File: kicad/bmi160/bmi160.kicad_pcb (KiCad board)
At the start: 2 copper layers, 31 x 42 mm, 41 parts, among them J1 USB4125-GF-A_REVA, J2 PinHeader_2x03_P2.54mm_Vertic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, J3 PinHeader_1x05_P2.54mm_Vertic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, J4 PinHeader_1x02_P2.54mm_Vertic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, SW1 SW_SPDT, U1 dfn-8_wide, U2 BQ297xy, U3 CSD85302L, U4 NCP177BMX330TCG, U5 ASAK-32.7680KHZ-LRS-T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

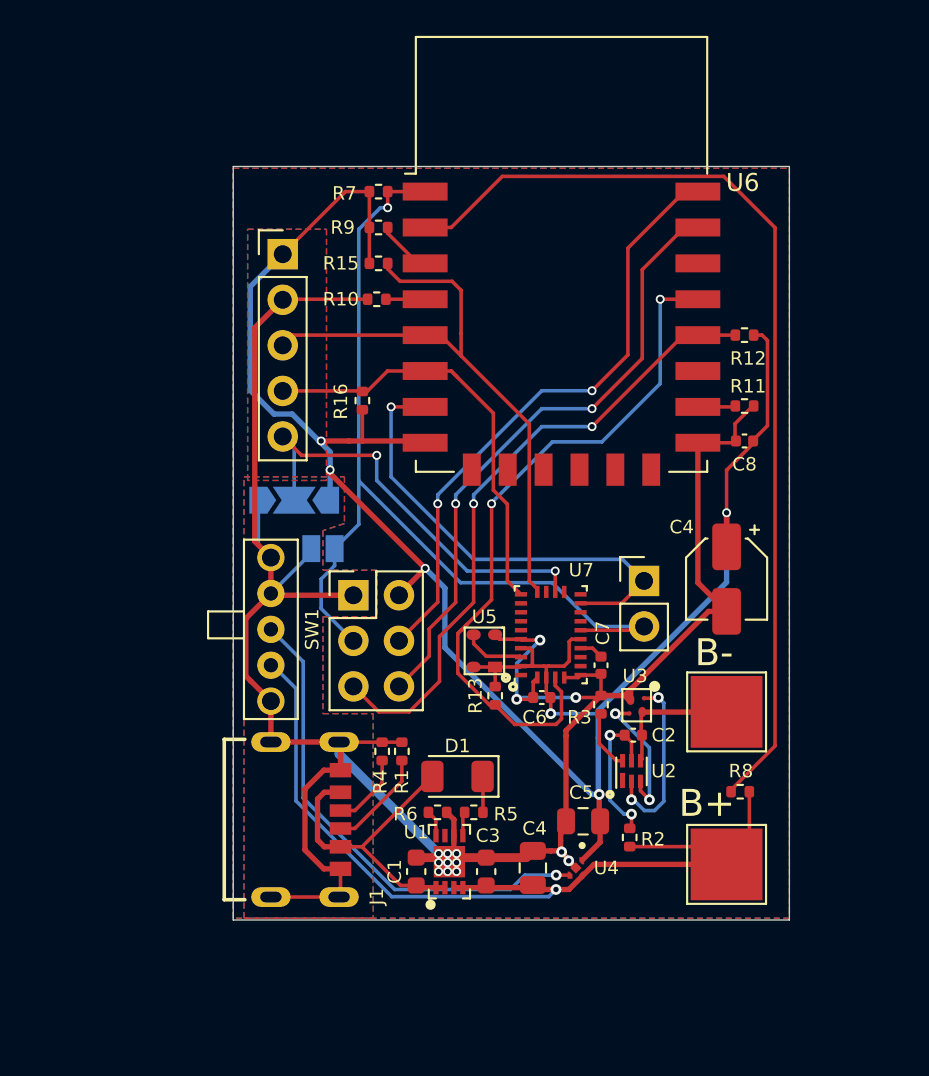
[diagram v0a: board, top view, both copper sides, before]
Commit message: added basic support for bmi160, it shold work i haven had a chance to test thogh
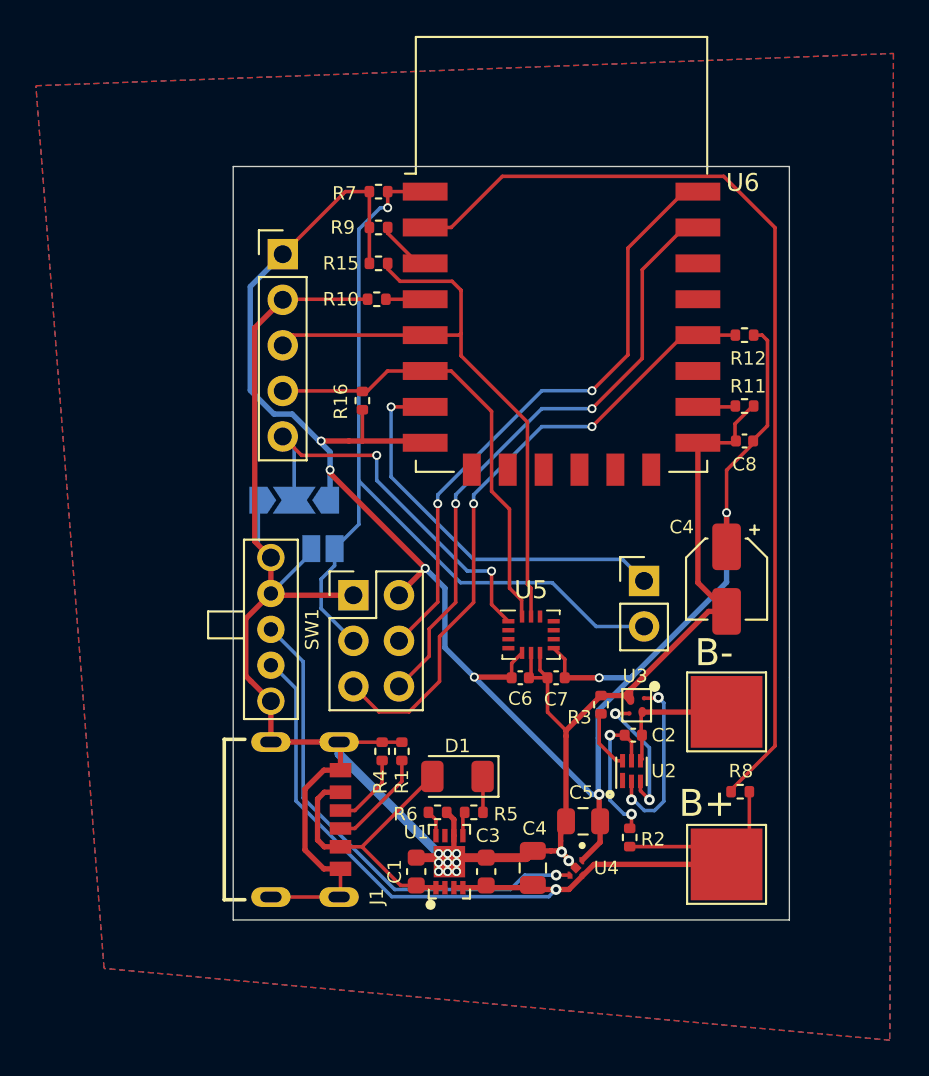
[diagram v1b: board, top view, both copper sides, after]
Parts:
- removed R13: 2.2k, Resistor_SMD:R_0402_1005Metric
- removed U7: BNO085, Package_LGA:LGA-28_5.2x3.8mm_P0.5mm
- U5: value ASAK-32.7680KHZ-LRS-T -> BMI160; footprint Oscillator:kc2016 -> Package_LGA:Bosch_LGA-14_3x2.5mm_P0.5mm
- moved U5 3.90 mm to (125.6, 93.6), turned to 0 degrees
- moved C7 2.60 mm to (127.0, 96.0), turned to 0 degrees
- moved C6 1.63 mm to (125.0, 96.0)
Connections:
- C6 pad 1: +3.3V -> GND
- C6 pad 2: GND -> +3.3V
- C7 pad 1: /CAP_BNO -> GND
- C7 pad 2: GND -> +3.3V
- J3 pad 5: /MOSI -> /ADDRESS
- JP1 pad 2: /MOSI -> /ADDRESS
- R12 pad 1: +3.3V -> /GPIO0
- R12 pad 2: /GPIO0 -> +3.3V
- R2 pad 1: /BAT_SENCE -> +BATT
- R2 pad 2: +BATT -> /BAT_SENCE
- U4 pad 5: GND -> (no net)
- U5 pad 1: +3.3V -> /ADDRESS
- U5 pad 2: GND -> unconnected-(U5-Pad2)
- U5 pad 3: /CLK_BNO -> unconnected-(U5-Pad3)
- U5 pad 4: +3.3V -> unconnected-(U5-Pad4)
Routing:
- net /BOOTN: track 38.9 -> 0.00 mm, vias 2 -> 0
- net /MOSI: track 24.1 -> 0.00 mm, vias 2 -> 0
- net /ADDRESS: track 0.00 -> 22.6 mm, vias 0 -> 2
- net GND: track 139.5 -> 130.3 mm, vias 14 -> 11
- net +3.3V: track 118.9 -> 112.8 mm, vias 6 -> 7
- net /INT: track 26.4 -> 22.3 mm
- net /CLK_BNO: track 3.45 -> 0.00 mm
- net /RESET: track 52.9 -> 49.6 mm
- net CH_PROG: track 0.00 -> 1.47 mm
- net /CH_PROG: track 1.47 -> 0.00 mm
- net /CAP_BNO: track 1.33 -> 0.00 mm
- net /H_SCL: track 34.1 -> 34.9 mm
- net /H_SDA: track 24.4 -> 25.2 mm
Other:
- board text added: "BMI ADDRESS"
- board text added: "BMI MODULE"
- board text added: "BMI PINS"
- board text added: "REV A"
- board text removed: "BNO ADDRESS"
- board text removed: "BNO MODULE"
- board text removed: "BNO PINS"
- board text removed: "REV D"
